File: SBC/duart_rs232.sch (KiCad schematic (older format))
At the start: 11 parts, among them J6 RS232a, J7 RS232b, U22 MAX238, U23 SC28L92PLCC44, X2 3.6864MHz

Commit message: Preparation for Pluto v3.0
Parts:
- C15, C16, C17, C18, C19: footprint Capacitors_ThroughHole:CP_Radial_Tantal_D4.5mm_P2.50mm -> Capacitor_THT:CP_Radial_Tantal_D4.5mm_P2.50mm; symbol device:CP1_Small -> pluto-rescue:CP1_Small-device
- C20: footprint Capacitors_ThroughHole:C_Disc_D4.7mm_W2.5mm_P5.00mm -> Capacitor_THT:C_Disc_D4.7mm_W2.5mm_P5.00mm; symbol device:C_Small -> pluto-rescue:C_Small-device
- J6, J7: footprint Connectors_IDC:IDC-Header_2x05_Pitch2.54mm_Straight -> Connector_IDC:IDC-Header_2x05_P2.54mm_Vertical; symbol conn:CONN_02X05 -> pluto-rescue:CONN_02X05-conn
- U22: footprint Housings_DIP:DIP-24_W7.62mm_Socket -> Package_DIP:DIP-24_W7.62mm_Socket
- X2: footprint Oscillators:Oscillator_DIP-8 -> Oscillator:Oscillator_DIP-8; symbol Oscillators:CXO_DIP8 -> pluto-rescue:CXO_DIP8-Oscillators
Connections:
- net labels added: ~DUART
- net labels removed: ~7FEX
- wire segments 89 -> 90
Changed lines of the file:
@@
 EESchema Schematic File Version 4
 LIBS:pluto-cache
-EELAYER 29 0
+EELAYER 30 0
 EELAYER END
 $Descr A4 11693 8268
@@
 F 0 "U22" H 4200 4250 50  0000 R CNN
 F 1 "MAX238" H 3825 3450 50  0000 R CNN
-F 2 "Housings_DIP:DIP-24_W7.62mm_Socket" H 3725 1750 50  0001 L CNN
+F 2 "Package_DIP:DIP-24_W7.62mm_Socket" H 3725 1750 50  0001 L CNN
 F 3 "" H 3675 3000 50  0001 C CNN
 	1    3675 2800
@@
 $EndComp
 $Comp
-L conn:CONN_02X05 J6
+L pluto-rescue:CONN_02X05-conn J6
 U 1 1 59ECCE48
 P 1500 2750
 F 0 "J6" H 1500 3050 50  0000 C CNN
 F 1 "RS232a" H 1500 2450 50  0000 C CNN
-F 2 "Connectors_IDC:IDC-Header_2x05_Pitch2.54mm_Straight" H 1500 1550 50  0001 C CNN
+F 2 "Connector_IDC:IDC-Header_2x05_P2.54mm_Vertical" H 1500 1550 50  0001 C CNN
 F 3 "" H 1500 1550 50  0001 C CNN
 	1    1500 2750
@@
 $EndComp
 $Comp
-L conn:CONN_02X05 J7
+L pluto-rescue:CONN_02X05-conn J7
 U 1 1 59ECCF01
 P 1500 3475
 F 0 "J7" H 1500 3775 50  0000 C CNN
 F 1 "RS232b" H 1500 3175 50  0000 C CNN
-F 2 "Connectors_IDC:IDC-Header_2x05_Pitch2.54mm_Straight" H 1500 2275 50  0001 C CNN
+F 2 "Connector_IDC:IDC-Header_2x05_P2.54mm_Vertical" H 1500 2275 50  0001 C CNN
 F 3 "" H 1500 2275 50  0001 C CNN
 	1    1500 3475
@@
 $EndComp
 $Comp
-L device:CP1_Small C18
+L pluto-rescue:CP1_Small-device C18
 U 1 1 59ECCF2A
 P 4650 1575
 F 0 "C18" H 4660 1645 50  0000 L CNN
 F 1 "1.0uF" H 4700 1500 50  0000 L CNN
-F 2 "Capacitors_ThroughHole:CP_Radial_Tantal_D4.5mm_P2.50mm" H 4650 1575 50  0001 C CNN
+F 2 "Capacitor_THT:CP_Radial_Tantal_D4.5mm_P2.50mm" H 4650 1575 50  0001 C CNN
 F 3 "" H 4650 1575 50  0001 C CNN
 	1    4650 1575
@@
 $EndComp
 $Comp
-L device:CP1_Small C19
+L pluto-rescue:CP1_Small-device C19
 U 1 1 59ECCF53
 P 4650 1975
 F 0 "C19" H 4660 2045 50  0000 L CNN
 F 1 "1.0uF" H 4700 1900 50  0000 L CNN
-F 2 "Capacitors_ThroughHole:CP_Radial_Tantal_D4.5mm_P2.50mm" H 4650 1975 50  0001 C CNN
+F 2 "Capacitor_THT:CP_Radial_Tantal_D4.5mm_P2.50mm" H 4650 1975 50  0001 C CNN
 F 3 "" H 4650 1975 50  0001 C CNN
 	1    4650 1975
@@
 $EndComp
 $Comp
-L device:CP1_Small C15
+L pluto-rescue:CP1_Small-device C15
 U 1 1 59ECCF86
 P 2750 1250
 F 0 "C15" H 2825 1325 50  0000 L CNN
 F 1 "1.0uF" H 2800 1175 50  0000 L CNN
-F 2 "Capacitors_ThroughHole:CP_Radial_Tantal_D4.5mm_P2.50mm" H 2750 1250 50  0001 C CNN
+F 2 "Capacitor_THT:CP_Radial_Tantal_D4.5mm_P2.50mm" H 2750 1250 50  0001 C CNN
 F 3 "" H 2750 1250 50  0001 C CNN
 	1    2750 1250
@@
 $EndComp
 $Comp
-L device:CP1_Small C16
+L pluto-rescue:CP1_Small-device C16
 U 1 1 59ECCFE5
 P 2750 1775
 F 0 "C16" H 2875 1850 50  0000 L CNN
 F 1 "1.0uF" H 2800 1700 50  0000 L CNN
-F 2 "Capacitors_ThroughHole:CP_Radial_Tantal_D4.5mm_P2.50mm" H 2750 1775 50  0001 C CNN
+F 2 "Capacitor_THT:CP_Radial_Tantal_D4.5mm_P2.50mm" H 2750 1775 50  0001 C CNN
 F 3 "" H 2750 1775 50  0001 C CNN
 	1    2750 1775
@@
 $EndComp
 $Comp
-L device:CP1_Small C17
+L pluto-rescue:CP1_Small-device C17
 U 1 1 59ECD006
 P 4325 1150
 F 0 "C17" V 4250 950 50  0000 L CNN
 F 1 "1.0uF" V 4400 900 50  0000 L CNN
-F 2 "Capacitors_ThroughHole:CP_Radial_Tantal_D4.5mm_P2.50mm" H 4325 1150 50  0001 C CNN
+F 2 "Capacitor_THT:CP_Radial_Tantal_D4.5mm_P2.50mm" H 4325 1150 50  0001 C CNN
 F 3 "" H 4325 1150 50  0001 C CNN
 	1    4325 1150
@@
 A[0..15]
 $Comp
-L device:C_Small C20
+L pluto-rescue:C_Small-device C20
 U 1 1 59ED58A6
 P 7475 5525
 F 0 "C20" V 7600 5475 50  0000 L CNN
 F 1 "0.1uF" V 7350 5450 50  0000 L CNN
-F 2 "Capacitors_ThroughHole:C_Disc_D4.7mm_W2.5mm_P5.00mm" H 7475 5525 50  0001 C CNN
+F 2 "Capacitor_THT:C_Disc_D4.7mm_W2.5mm_P5.00mm" H 7475 5525 50  0001 C CNN
 F 3 "" H 7475 5525 50  0001 C CNN
 	1    7475 5525
@@
 	8575 4625 7650 4625
 Text HLabel 8575 4250 2    60   Input ~ 0
-~7FEX
+~DUART
 Wire Wire Line
 	8575 4250 7650 4250
 NoConn ~ 7650 5000
 $Comp
-L Oscillators:CXO_DIP8 X2
+L pluto-rescue:CXO_DIP8-Oscillators X2
 U 1 1 59EDF126
 P 9675 4875
 F 0 "X2" H 9475 5125 50  0000 L CNN
 F 1 "3.6864MHz" H 9175 4600 50  0000 L CNN
-F 2 "Oscillators:Oscillator_DIP-8" H 10125 4525 50  0001 C CNN
+F 2 "Oscillator:Oscillator_DIP-8" H 10125 4525 50  0001 C CNN
 F 3 "" H 9575 4875 50  0001 C CNN
 	1    9675 4875
@@
 L power:VCC #PWR049
 U 1 1 59EE01CB
-P 9675 4575
-F 0 "#PWR049" H 9675 4425 50  0001 C CNN
-F 1 "VCC" H 9675 4725 50  0000 C CNN
-F 2 "" H 9675 4575 50  0001 C CNN
-F 3 "" H 9675 4575 50  0001 C CNN
-	1    9675 4575
+P 9675 4475
+F 0 "#PWR049" H 9675 4325 50  0001 C CNN
+F 1 "VCC" H 9675 4625 50  0000 C CNN
+F 2 "" H 9675 4475 50  0001 C CNN
+F 3 "" H 9675 4475 50  0001 C CNN
+	1    9675 4475
 	1    0    0    -1
 $EndComp
@@
 Wire Wire Line
 	3675 1150 4225 1150
+Wire Wire Line
+	9675 4575 9675 4475
 Wire Bus Line
 	8075 3350 8075 3850

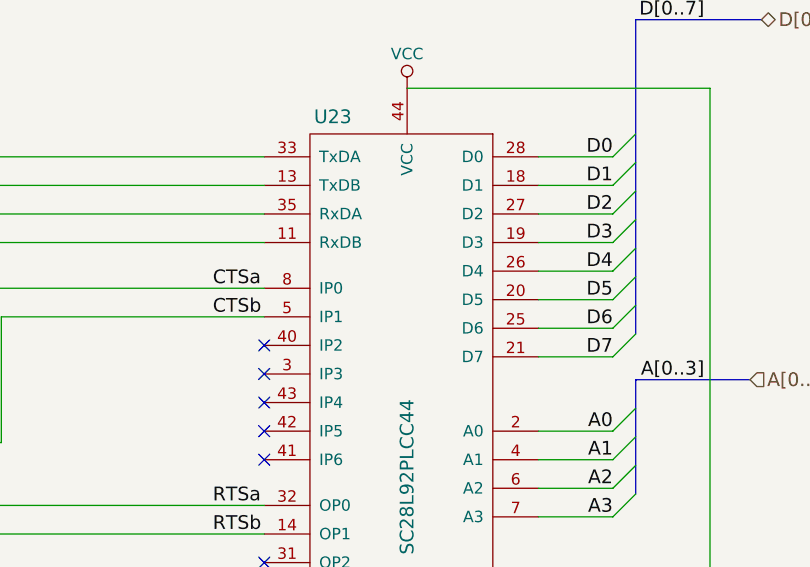
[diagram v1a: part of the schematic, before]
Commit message: A better layout of PCB.
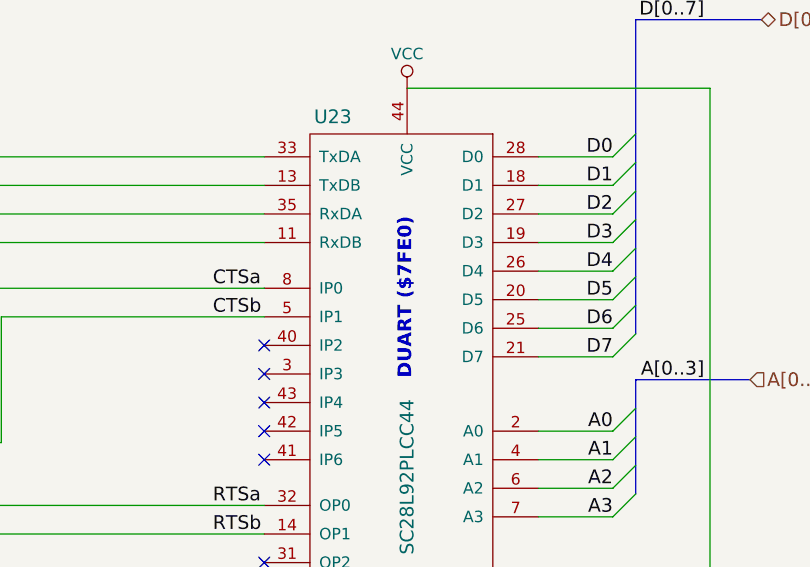
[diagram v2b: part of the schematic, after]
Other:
- note added: "DUART ($7FE0)"
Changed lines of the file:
@@
 Wire Bus Line
 	8075 1775 8075 3150
+Text Notes 7100 3350 1    60   ~ 12
+DUART ($7FE0)
 $EndSCHEMATC

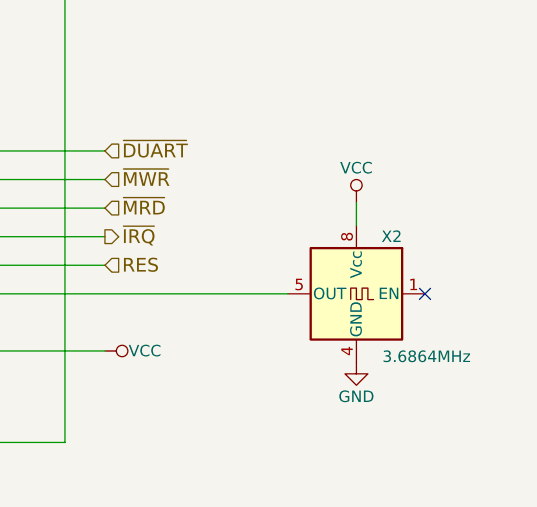
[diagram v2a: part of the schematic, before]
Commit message: Converting to SMD of almost all components.
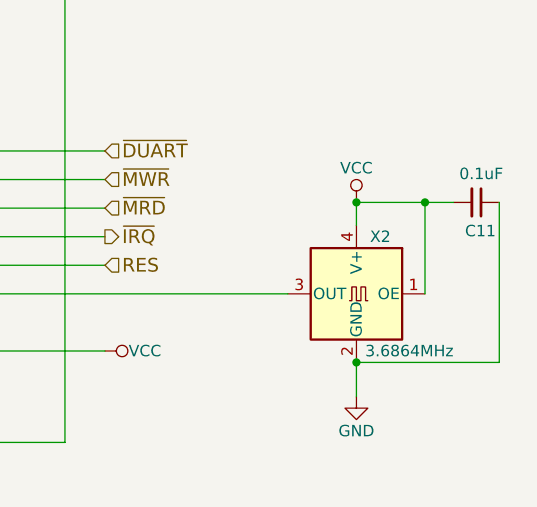
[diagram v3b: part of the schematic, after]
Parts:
- removed X2: 3.6864MHz, Oscillator:Oscillator_DIP-8, symbol pluto-rescue:CXO_DIP8-Oscillators
- added C11: 0.1uF, Capacitor_SMD:C_0603_1608Metric_Pad1.05x0.95mm_HandSolder, symbol pluto-rescue:C_Small-device
- added X2: 3.6864MHz, Oscillator:Oscillator_SMD_SeikoEpson_SG8002CA-4Pin_7.0x5.0mm, symbol Oscillator:SG-8002CA
- C15, C16, C17, C18, C19: footprint Capacitor_THT:CP_Radial_Tantal_D4.5mm_P2.50mm -> Capacitor_Tantalum_SMD:CP_EIA-3528-21_Kemet-B_Pad1.50x2.35mm_HandSolder
- C20: footprint Capacitor_THT:C_Disc_D4.7mm_W2.5mm_P5.00mm -> Capacitor_SMD:C_0603_1608Metric_Pad1.05x0.95mm_HandSolder
- U22: footprint Package_DIP:DIP-24_W7.62mm_Socket -> Package_SO:SOIC-24W_7.5x15.4mm_P1.27mm
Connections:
- net GND: now also C11.1, X2.2 (GND)
- net VCC: now also C11.2, X2.1 (OE), X2.4 (V+)
- net at U23.36 (X1/CLK): now also X2.3 (OUT)
- no-connect marks 23 -> 22
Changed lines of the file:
@@
 F 0 "U22" H 4200 4250 50  0000 R CNN
 F 1 "MAX238" H 3825 3450 50  0000 R CNN
-F 2 "Package_DIP:DIP-24_W7.62mm_Socket" H 3725 1750 50  0001 L CNN
+F 2 "Package_SO:SOIC-24W_7.5x15.4mm_P1.27mm" H 3725 1750 50  0001 L CNN
 F 3 "" H 3675 3000 50  0001 C CNN
 	1    3675 2800
@@
 F 0 "C18" H 4660 1645 50  0000 L CNN
 F 1 "1.0uF" H 4700 1500 50  0000 L CNN
-F 2 "Capacitor_THT:CP_Radial_Tantal_D4.5mm_P2.50mm" H 4650 1575 50  0001 C CNN
+F 2 "Capacitor_Tantalum_SMD:CP_EIA-3528-21_Kemet-B_Pad1.50x2.35mm_HandSolder" H 4650 1575 50  0001 C CNN
 F 3 "" H 4650 1575 50  0001 C CNN
 	1    4650 1575
@@
 F 0 "C19" H 4660 2045 50  0000 L CNN
 F 1 "1.0uF" H 4700 1900 50  0000 L CNN
-F 2 "Capacitor_THT:CP_Radial_Tantal_D4.5mm_P2.50mm" H 4650 1975 50  0001 C CNN
+F 2 "Capacitor_Tantalum_SMD:CP_EIA-3528-21_Kemet-B_Pad1.50x2.35mm_HandSolder" H 4650 1975 50  0001 C CNN
 F 3 "" H 4650 1975 50  0001 C CNN
 	1    4650 1975
@@
 F 0 "C15" H 2825 1325 50  0000 L CNN
 F 1 "1.0uF" H 2800 1175 50  0000 L CNN
-F 2 "Capacitor_THT:CP_Radial_Tantal_D4.5mm_P2.50mm" H 2750 1250 50  0001 C CNN
+F 2 "Capacitor_Tantalum_SMD:CP_EIA-3528-21_Kemet-B_Pad1.50x2.35mm_HandSolder" H 2750 1250 50  0001 C CNN
 F 3 "" H 2750 1250 50  0001 C CNN
 	1    2750 1250
@@
 F 0 "C16" H 2875 1850 50  0000 L CNN
 F 1 "1.0uF" H 2800 1700 50  0000 L CNN
-F 2 "Capacitor_THT:CP_Radial_Tantal_D4.5mm_P2.50mm" H 2750 1775 50  0001 C CNN
+F 2 "Capacitor_Tantalum_SMD:CP_EIA-3528-21_Kemet-B_Pad1.50x2.35mm_HandSolder" H 2750 1775 50  0001 C CNN
 F 3 "" H 2750 1775 50  0001 C CNN
 	1    2750 1775
@@
 F 0 "C17" V 4250 950 50  0000 L CNN
 F 1 "1.0uF" V 4400 900 50  0000 L CNN
-F 2 "Capacitor_THT:CP_Radial_Tantal_D4.5mm_P2.50mm" H 4325 1150 50  0001 C CNN
+F 2 "Capacitor_Tantalum_SMD:CP_EIA-3528-21_Kemet-B_Pad1.50x2.35mm_HandSolder" H 4325 1150 50  0001 C CNN
 F 3 "" H 4325 1150 50  0001 C CNN
 	1    4325 1150
@@
 F 0 "C20" V 7600 5475 50  0000 L CNN
 F 1 "0.1uF" V 7350 5450 50  0000 L CNN
-F 2 "Capacitor_THT:C_Disc_D4.7mm_W2.5mm_P5.00mm" H 7475 5525 50  0001 C CNN
+F 2 "Capacitor_SMD:C_0603_1608Metric_Pad1.05x0.95mm_HandSolder" H 7475 5525 50  0001 C CNN
 F 3 "" H 7475 5525 50  0001 C CNN
 	1    7475 5525
@@
 NoConn ~ 7650 5000
 $Comp
-L pluto-rescue:CXO_DIP8-Oscillators X2
-U 1 1 59EDF126
-P 9675 4875
-F 0 "X2" H 9475 5125 50  0000 L CNN
-F 1 "3.6864MHz" H 9175 4600 50  0000 L CNN
-F 2 "Oscillator:Oscillator_DIP-8" H 10125 4525 50  0001 C CNN
-F 3 "" H 9575 4875 50  0001 C CNN
-	1    9675 4875
-	-1   0    0    -1
-$EndComp
-$Comp
 L power:VCC #PWR049
 U 1 1 59EE01CB
@@
 L power:GND #PWR050
 U 1 1 59EE022C
-P 9675 5175
-F 0 "#PWR050" H 9675 4925 50  0001 C CNN
-F 1 "GND" H 9675 5025 50  0000 C CNN
-F 2 "" H 9675 5175 50  0001 C CNN
-F 3 "" H 9675 5175 50  0001 C CNN
-	1    9675 5175
+P 9675 5325
+F 0 "#PWR050" H 9675 5075 50  0001 C CNN
+F 1 "GND" H 9675 5175 50  0000 C CNN
+F 2 "" H 9675 5325 50  0001 C CNN
+F 3 "" H 9675 5325 50  0001 C CNN
+	1    9675 5325
 	1    0    0    -1
 $EndComp
@@
 Wire Wire Line
 	8575 5125 7650 5125
-NoConn ~ 9975 4875
 NoConn ~ 1250 2550
 NoConn ~ 1750 2650
@@
 Wire Wire Line
 	9675 4575 9675 4475
+Text Notes 7100 3350 1    60   ~ 12
+DUART ($7FE0)
+$Comp
+L Oscillator:SG-8002CA X2
+U 1 1 5D6A4602
+P 9675 4875
+F 0 "X2" H 9525 5125 50  0000 L CNN
+F 1 "3.6864MHz" H 9250 4625 50  0000 L CNN
+F 2 "Oscillator:Oscillator_SMD_SeikoEpson_SG8002CA-4Pin_7.0x5.0mm" H 10375 4525 50  0001 C CNN
+F 3 "https://support.epson.biz/td/api/doc_check.php?mode=dl&lang=en&Parts=SG-8002DC" H 9575 4875 50  0001 C CNN
+	1    9675 4875
+	-1   0    0    -1
+$EndComp
+Wire Wire Line
+	9675 5175 9675 5325
+Wire Wire Line
+	9975 4875 9975 4475
+Wire Wire Line
+	9975 4475 9675 4475
+Connection ~ 9675 4475
+$Comp
+L pluto-rescue:C_Small-device C11
+U 1 1 5D6B187A
+P 10200 4475
+F 0 "C11" V 10325 4425 50  0000 L CNN
+F 1 "0.1uF" V 10075 4400 50  0000 L CNN
+F 2 "Capacitor_SMD:C_0603_1608Metric_Pad1.05x0.95mm_HandSolder" H 10200 4475 50  0001 C CNN
+F 3 "" H 10200 4475 50  0001 C CNN
+	1    10200 4475
+	0    1    1    0
+$EndComp
+Wire Wire Line
+	9975 4475 10100 4475
+Connection ~ 9975 4475
+Wire Wire Line
+	10300 4475 10300 5175
+Wire Wire Line
+	10300 5175 9675 5175
+Connection ~ 9675 5175
 Wire Bus Line
 	8075 3350 8075 3850
 Wire Bus Line
 	8075 1775 8075 3150
-Text Notes 7100 3350 1    60   ~ 12
-DUART ($7FE0)
 $EndSCHEMATC

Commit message: New PCB layout is taking shape.
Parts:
- C11, C20: footprint Capacitor_SMD:C_0603_1608Metric_Pad1.05x0.95mm_HandSolder -> Capacitor_SMD:C_0805_2012Metric_Pad1.15x1.40mm_HandSolder
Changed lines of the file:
@@
 F 0 "C20" V 7600 5475 50  0000 L CNN
 F 1 "0.1uF" V 7350 5450 50  0000 L CNN
-F 2 "Capacitor_SMD:C_0603_1608Metric_Pad1.05x0.95mm_HandSolder" H 7475 5525 50  0001 C CNN
+F 2 "Capacitor_SMD:C_0805_2012Metric_Pad1.15x1.40mm_HandSolder" H 7475 5525 50  0001 C CNN
 F 3 "" H 7475 5525 50  0001 C CNN
 	1    7475 5525
@@
 F 0 "C11" V 10325 4425 50  0000 L CNN
 F 1 "0.1uF" V 10075 4400 50  0000 L CNN
-F 2 "Capacitor_SMD:C_0603_1608Metric_Pad1.05x0.95mm_HandSolder" H 10200 4475 50  0001 C CNN
+F 2 "Capacitor_SMD:C_0805_2012Metric_Pad1.15x1.40mm_HandSolder" H 10200 4475 50  0001 C CNN
 F 3 "" H 10200 4475 50  0001 C CNN
 	1    10200 4475
